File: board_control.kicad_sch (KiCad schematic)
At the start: 47 parts, among them J10 Conn_01x02_Pin, J4 Conn_01x09_Pin

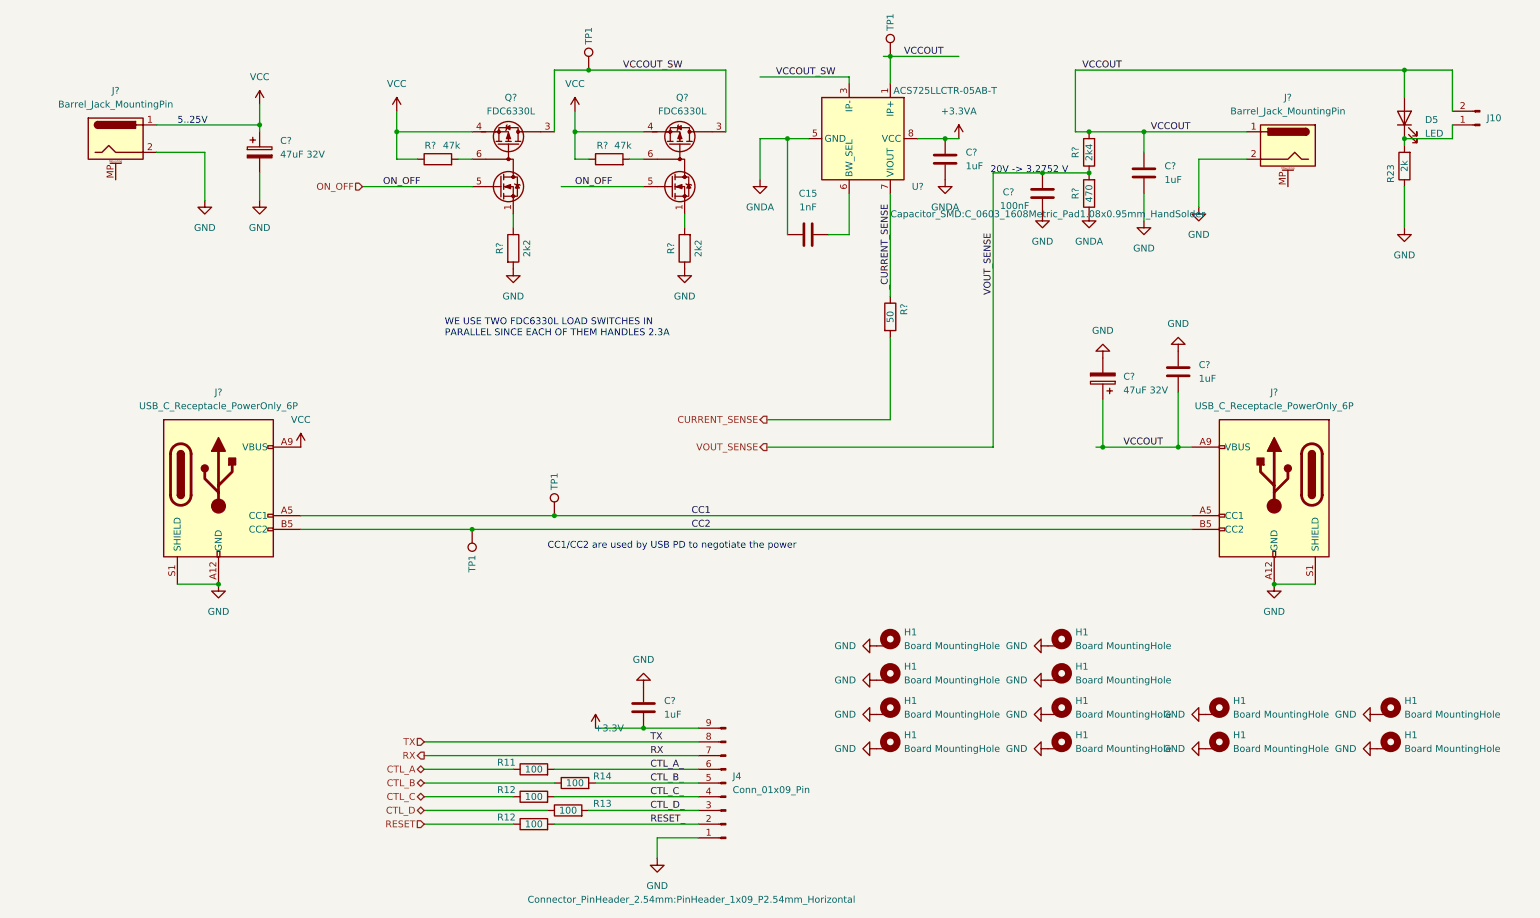
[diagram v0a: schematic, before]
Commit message: Reorganized repo with rename to dutlink 1.1.0
Signed-off-by: Miguel Angel Ajo Pelayo <majopela@redhat.com>
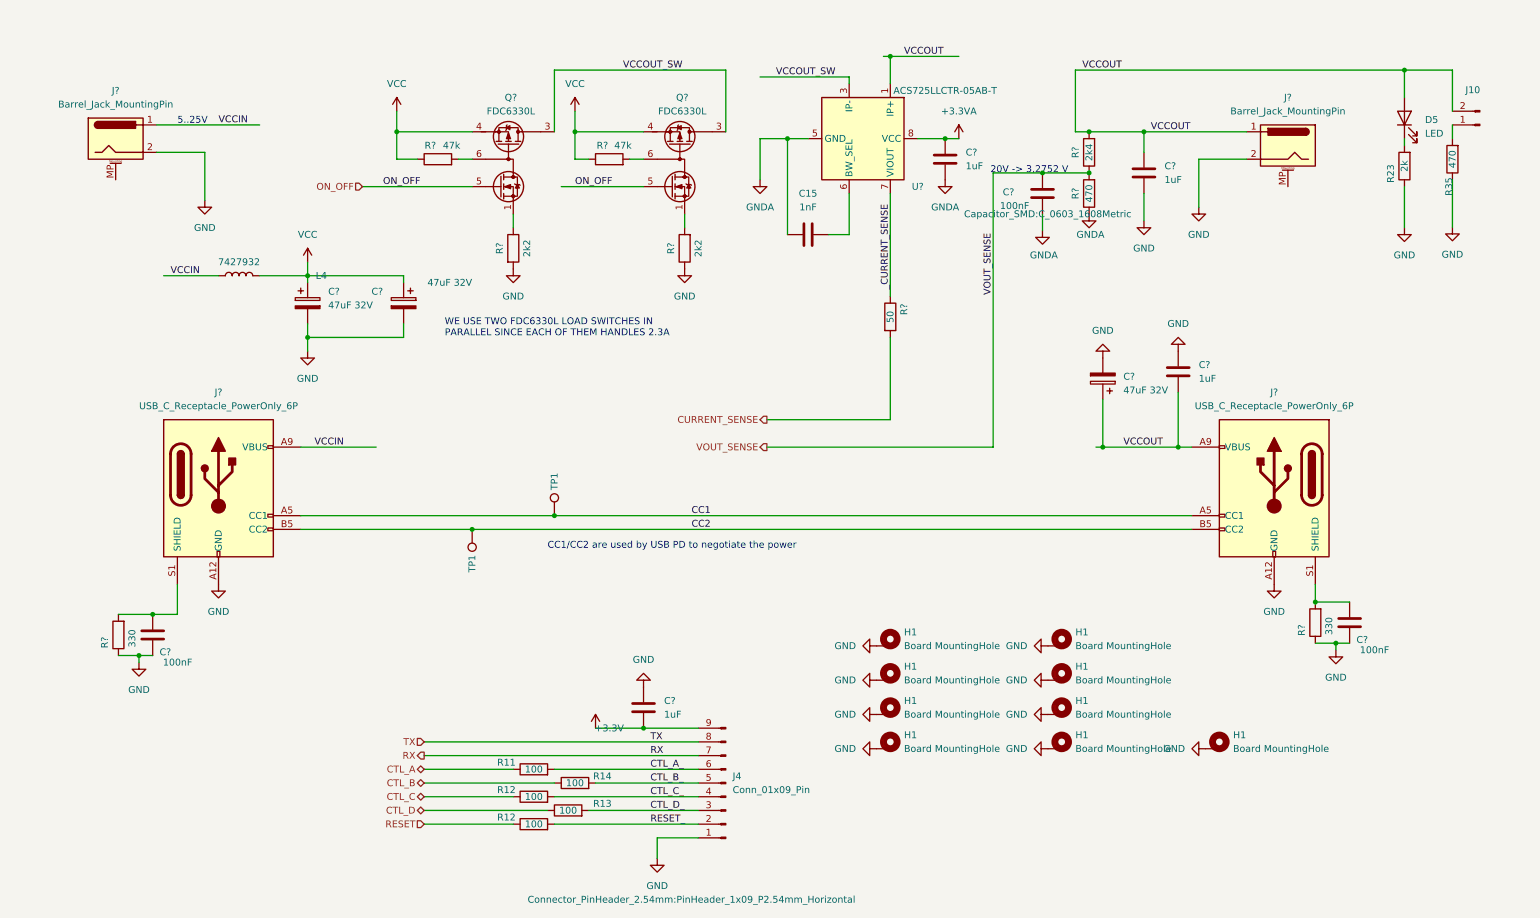
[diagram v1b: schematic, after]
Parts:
- removed C?: 47uF 32V, Capacitor_SMD:CP_Elec_6.3x5.4_Nichicon, symbol Device:C_Polarized
- removed H1 (x3): Board MountingHole, MountingHole:MountingHole_2.7mm_M2.5_Pad_Via, symbol Mechanical:MountingHole
- removed TP1 (x2): TestPoint, TestPoint:TestPoint_Pad_D1.0mm, symbol Connector:TestPoint
- added C? (x2): 47uF 32V, Capacitor_SMD:CP_Elec_6.3x5.4_Nichicon, symbol Device:C_Polarized
- added C? (x2): 100nF, Capacitor_SMD:C_0603_1608Metric, symbol Device:C
- added L4: 7427932, FOOTPRINTS:7427932, symbol Device:L
- added R35: 470, Resistor_SMD:R_0603_1608Metric, symbol Device:R
- added R? (x2): 330, Resistor_SMD:R_0402_1005Metric, symbol Device:R
- C15, C? (x4): footprint Capacitor_SMD:C_0603_1608Metric_Pad1.08x0.95mm_HandSolder -> Capacitor_SMD:C_0603_1608Metric; MFN (none) -> CL10B105KA8NNNC
- C?: footprint Capacitor_SMD:C_0603_1608Metric_Pad1.08x0.95mm_HandSolder -> Capacitor_SMD:C_0603_1608Metric; MFN (none) -> CL10B104KB8NNNC
- C?: MFN (none) -> HV470M035E055ETR
- D5: MFN (none) -> LTST-C190KRKT
- J10: MFN (none) -> PZ254V-11-02P
- J4: MFN (none) -> A2541WR-9P
- J? (x2): footprint Connector_USB:USB_C_Receptacle_G-Switch_GT-USB-7010ASV -> FOOTPRINTS:USB_C_Receptacle_G-Switch_GT-USB-7010ASV_fix; MFN (none) -> GT-USB-7010ASV
- J? (x2): MFN (none) -> DC-005B-2.5A-2.5
- Q? (x2): MFN (none) -> FDC6330L
- R11, R12, R13, R14: MFN (none) -> RTT031000FTP
- R23: MFN (none) -> RC0603FR-072KL
- R?: MFN (none) -> RC0603FR-072K4L
- R? (x2): MFN (none) -> RC0603JR-0747KL
- R?: MFN (none) -> RC0603JR-07470RL
- R?: MFN (none) -> RT0603BRE0750RL
- R? (x2): MFN (none) -> RC0603FR-072K2L
- U?: Link (none) -> https://www.mouser.es/ProductDetail/onsemi-Fairchild/FDC633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; MFN (none) -> ACS725LLCTR-05AB-T
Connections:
- net GND: now also C?.2, C?.2, C?.2, C?.2, R35.1, R?.1, R?.1; no longer C?.2, J?.S1 (SHIELD), J?.S1 (SHIELD)
- net GNDA: now also C?.2
- net VCC: now also C?.1, C?.1, L4.2; no longer J?.1, J?.A9 (VBUS), J?.B9 (VBUS)
- net at D5.1 (K), R23.2: no longer J10.1 (Pin_1)
- new net: J10.1 (Pin_1), R35.2
- new net: C?.1, J?.S1 (SHIELD), R?.2 (x2)
- new net VCCIN: J?.1, J?.A9 (VBUS), J?.B9 (VBUS), L4.1

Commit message: 2.0.0 release
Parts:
- removed C? (x2): 47uF 32V, Capacitor_SMD:CP_Elec_6.3x5.4_Nichicon, symbol Device:C_Polarized
- removed C? (x2): 100nF, Capacitor_SMD:C_0603_1608Metric, symbol Device:C
- removed R35: 470, Resistor_SMD:R_0603_1608Metric, symbol Device:R
- removed R? (x2): 330, Resistor_SMD:R_0402_1005Metric, symbol Device:R
- added C? (x2): 47uF 32V, Capacitor_SMD:CP_Elec_6.3x5.4_Nichicon, symbol Device:C_Polarized
- added C? (x2): 100nF, Capacitor_SMD:C_0402_1005Metric, symbol Device:C
- added H1: Board MountingHole, MountingHole:MountingHole_2.7mm_M2.5_Pad_Via, symbol Mechanical:MountingHole
- added J20: SPI/TPM connector, Connector_PinHeader_2.54mm:PinHeader_2x05_P2.54mm_Vertical, symbol Connector_Generic:Conn_02x05_Odd_Even
- added R23: 2k, Resistor_SMD:R_0402_1005Metric, symbol Device:R
- added R? (x2): 330, Resistor_SMD:R_0402_1005Metric, symbol Device:R
- added TP1: TestPoint, TestPoint:TestPoint_Pad_D1.0mm, symbol Connector:TestPoint
- C15: footprint Capacitor_SMD:C_0603_1608Metric -> Capacitor_SMD:C_0402_1005Metric; Link (none) -> https://eu.mouser.com/ProductDetail/YAGEO/CC0402KRX7R0BB102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; MFN CL10B105KA8NNNC -> CC0402KRX7R0BB102; MPN (none) -> CC0402KRX7R0BB102
- C? (x4): MPN (none) -> CL10B105KA8NNNC
- C?: footprint Capacitor_SMD:C_0603_1608Metric -> Capacitor_SMD:C_0402_1005Metric; MPN (none) -> CL05B104K05NNNC; MPN2 (none) -> TCC0402X7R104M160AT
- C?: MPN (none) -> HV470M035E055ETR
- D5: MPN (none) -> LTST-C190KRKT
- J10: MPN (none) -> PZ254V-11-02P
- J4: MPN (none) -> A2541WR-9P
- J? (x2): Link (none) -> https://www.lcsc.com/product-detail/USB-Connectors_G-Switch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; MPN (none) -> GT-USB-7010ASV
- J? (x2): MPN (none) -> DC-005B-2.5A-2.5
- Q? (x2): Link (none) -> https://www.mouser.es/ProductDetail/onsemi-Fairchild/FDC633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; MPN (none) -> FDC6330L
- R11, R12, R13, R14: footprint Resistor_SMD:R_0603_1608Metric -> Resistor_SMD:R_0402_1005Metric; MFN RTT031000FTP -> RTT021000FTH; MPN (none) -> RTT021000FTH
- R23: footprint Resistor_SMD:R_0603_1608Metric -> Resistor_SMD:R_0402_1005Metric; MFN RC0603FR-072KL -> RTT02202JTH; MPN (none) -> RTT02202JTH
- R?: value 2k4 -> 2k4 1%; footprint Resistor_SMD:R_0603_1608Metric -> Resistor_SMD:R_0402_1005Metric; MFN RC0603FR-072K4L -> AC0402FR-072K4L; MPN (none) -> AC0402FR-072K4L
- R? (x2): footprint Resistor_SMD:R_0603_1608Metric -> Resistor_SMD:R_0402_1005Metric; MFN RC0603JR-0747KL -> RTT024702FTH; MPN (none) -> RTT024702FTH
- R?: value 470 -> 470 1%; footprint Resistor_SMD:R_0603_1608Metric -> Resistor_SMD:R_0402_1005Metric; MFN RC0603JR-07470RL -> RTT024700FTH; MPN (none) -> RTT024700FTH
- R?: footprint Resistor_SMD:R_0603_1608Metric -> Resistor_SMD:R_0402_1005Metric; MFN RT0603BRE0750RL -> RC0402JR-0750RL; MPN (none) -> RC0402JR-0750RL
- R? (x2): footprint Resistor_SMD:R_0603_1608Metric -> Resistor_SMD:R_0402_1005Metric; MFN RC0603FR-072K2L -> RTT022201FTH; MPN (none) -> RTT022201FTH
- U?: Link https://www.mouser.es/ProductDetail/onsemi-Fairchild/FDC633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 -> https://eu.mouser.com/ProductDetail/Allegro-MicroSystems/AC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; MPN (none) -> ACS725LLCTR-05AB-T
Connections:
- net GND: now also C?.2, C?.2, C?.2, C?.2, H1.1, R23.1, R?.1, R?.1
- net VCC: now also C?.1
- net VCCOUT: now also TP1.1
- net at J10.1 (Pin_1): now also R23.2
- net at J?.S1 (SHIELD): now also C?.1, R?.2 (x2)
- net VCCIN renamed J1_VCC
- net J1_VCC: now also J20.3 (Pin_3); no longer J?.1, L4.1
- new net J2_VCC: J20.1 (Pin_1), J?.1
- new net V_IN_ATX12: J20.5 (Pin_5)
- new net V_IN_ATX5: J20.7 (Pin_7), J20.9 (Pin_9)
- new net _VCC: C?.1, J20.10 (Pin_10), J20.2 (Pin_2), J20.4 (Pin_4), J20.6 (Pin_6), J20.8 (Pin_8), L4.1
- no-connect marks 0 -> 2
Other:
- moved on the sheet: J?
